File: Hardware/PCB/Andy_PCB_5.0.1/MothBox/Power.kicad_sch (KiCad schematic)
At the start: 31 parts, among them J1 DB141V-2.54-4P, J2 DB141V-2.54-4P, J3 DB141V-2.54-4P, Q1 JMTV210P02A, Q2 AO3400A, Q8 JMTV210P02A, U1 Place Holder voltage regulator, U2 XL4015E1, U3 INA219BIDCNT

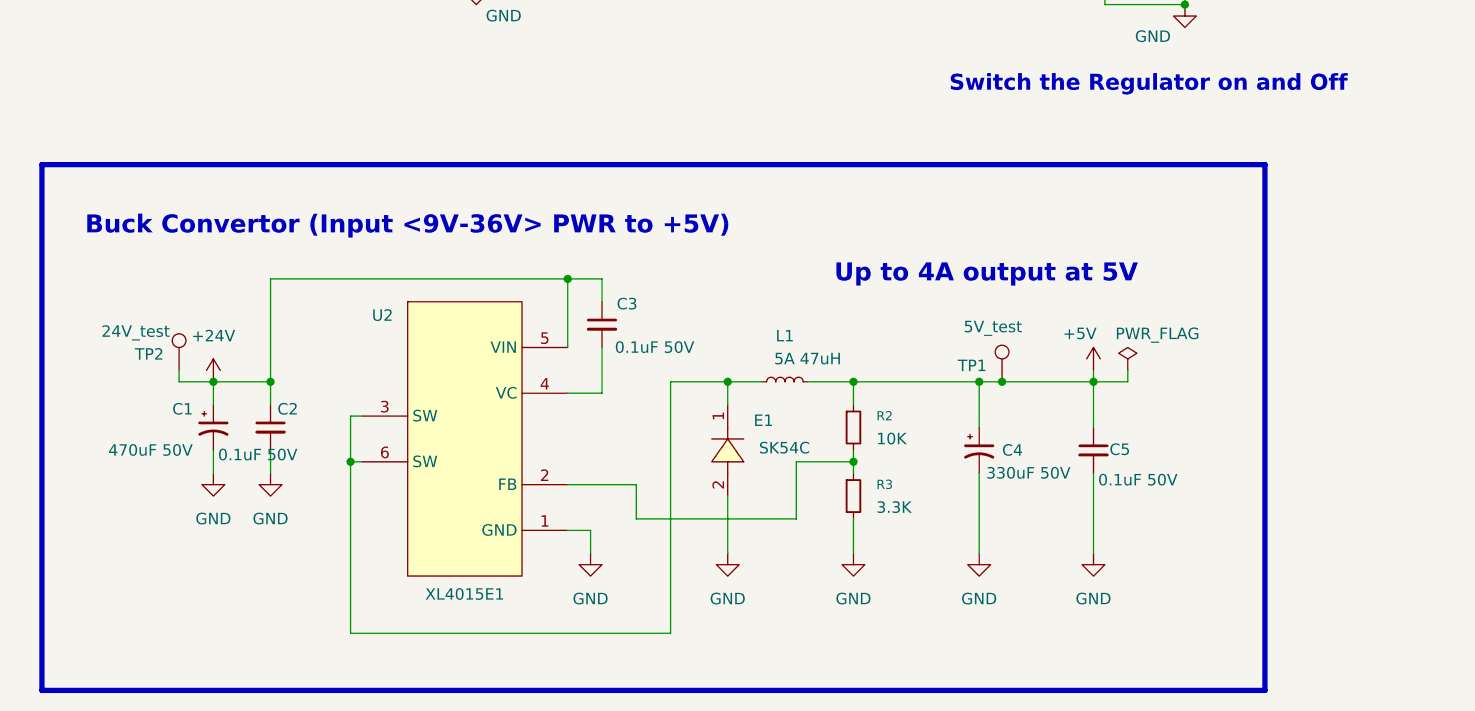
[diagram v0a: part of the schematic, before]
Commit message: added in extra hour switch for 24hr coverage
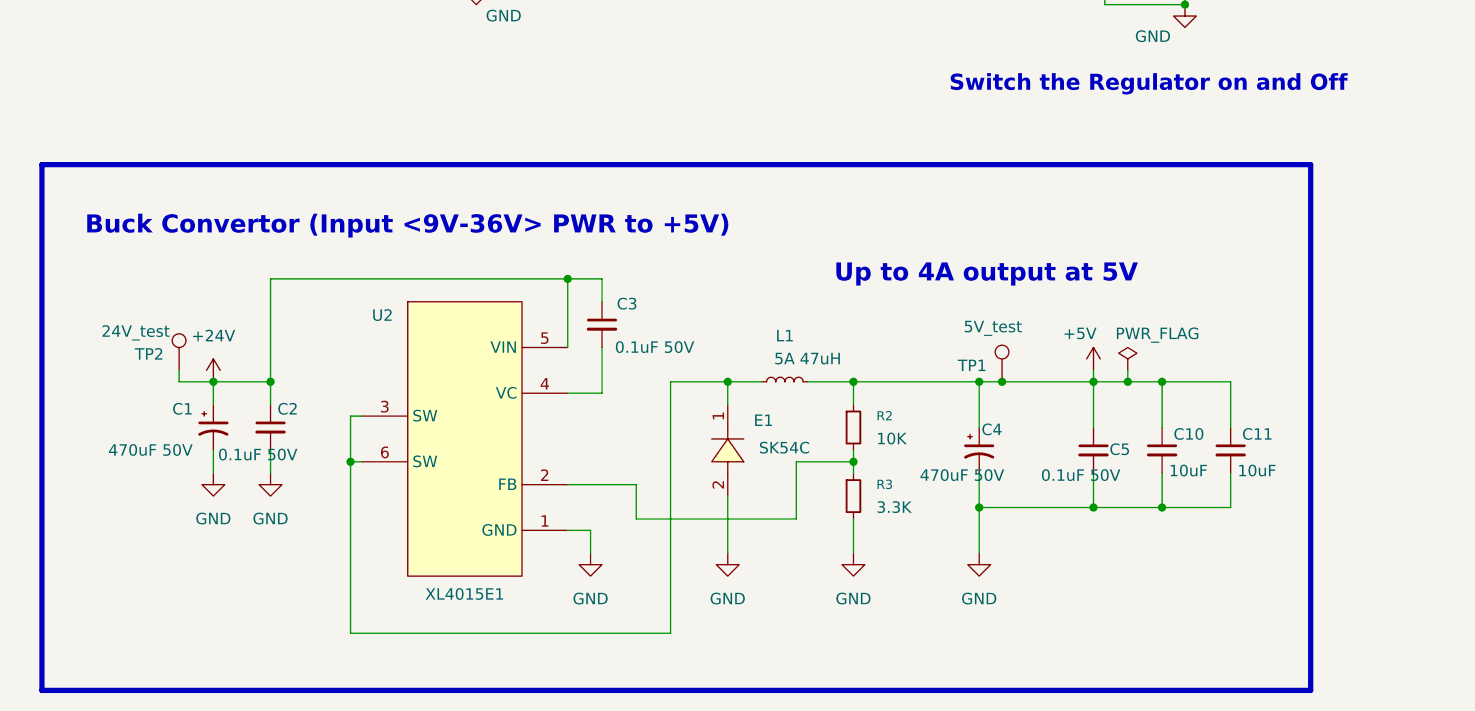
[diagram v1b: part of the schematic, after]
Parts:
- added C10, C11: 10uF, MothBox_footprints_Library:C_0603_1608Metric, symbol MothBox_Symbol_Library:C_Small
- C1: LCSC_Part (none) -> C90272; LCSC_Part_No C90272 -> (none)
- C2, C3, C5: footprint MothBox_footprints_Library:R_0603_1608Metric -> MothBox_footprints_Library:C_0603_1608Metric; LCSC_Part (none) -> C14663; LCSC_Part_No C3011704 -> (none)
- C4: value 330uF 50V -> 470uF 50V; footprint MothBox_footprints_Library:CP_Elec_10x10 -> MothBox_footprints_Library:CP_Elec_10x12.5; LCSC_Part (none) -> C90272; LCSC_Part_No C2687701 -> (none)
- C6: LCSC C14663 -> (none); LCSC_Part (none) -> C14663; LCSC_Part_No C3011704 -> (none)
- C8: LCSC_Part (none) -> C19702
- D1: LCSC C571388 -> (none); LCSC_Part (none) -> C571388
- E1: LCSC_Part_No C5449119 -> (none)
- F2: LCSC C7500481 -> (none); LCSC_Part (none) -> C7500481
- J1, J2, J3: LCSC C2898746 -> (none); LCSC_Part (none) -> C2898746
- L1: LCSC_Part (none) -> C497913; LCSC_Part_No C497913 -> (none)
- Q1, Q8: LCSC_Part (none) -> C2938482
- Q2: LCSC C2938367 -> (none); LCSC_Part (none) -> C2938367
- R1, R29, R30: LCSC_Part (none) -> C25804
- R2: footprint MothBox_footprints_Library:R_0805_2012Metric -> MothBox_footprints_Library:R_0603_1608Metric; LCSC_Part (none) -> C25804; LCSC_Part_No C84376 -> (none)
- R3: footprint MothBox_footprints_Library:R_0805_2012Metric -> MothBox_footprints_Library:R_0603_1608Metric; LCSC_Part (none) -> C22978; LCSC_Part_No C114531 -> (none)
- R5, R6: LCSC_Part C2930027 -> C23162
- TP1, TP2, TP5: now left out of the parts list
- U2: LCSC_Part_No C51661 -> (none)
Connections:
- net +5V: now also C10.1, C11.1
- net GND: now also C10.2, C11.2

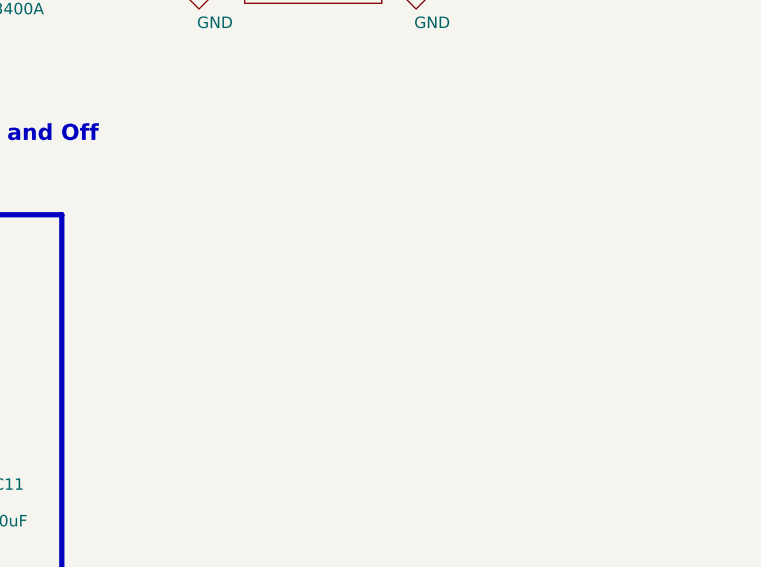
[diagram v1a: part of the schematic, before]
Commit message: MothBox PCB updated and sent off for production. MothBeam edge edits and sent off for second production for Parkview
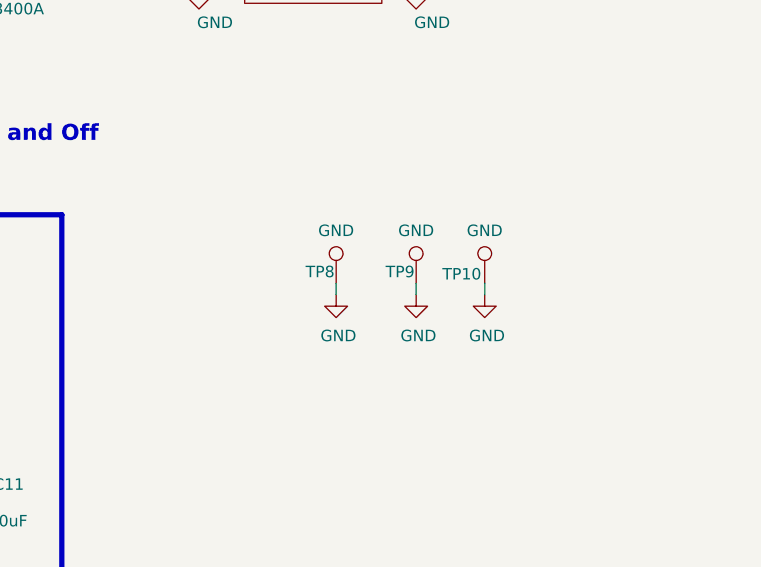
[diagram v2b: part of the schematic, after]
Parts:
- added TP10, TP8, TP9: GND, MothBox_footprints_Library:TestPoint_THTPad_D1.0mm_Drill0.5mm, symbol MothBox_Symbol_Library:TestPoint
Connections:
- net GND: now also TP10.1, TP8.1, TP9.1
